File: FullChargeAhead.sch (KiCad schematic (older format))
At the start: 18 parts, among them P101 USB_OTG, P102 CONN_01X02, U101 MCP73834

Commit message: starting rev 2
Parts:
- removed D103: NOPOP, LEDs:LED_0805, symbol LED
- removed R106: NOPOP, Resistors_SMD:R_0805_HandSoldering, symbol R
- removed R108: 0R, Resistors_SMD:R_0805_HandSoldering, symbol R
- removed TH101: THERMISTOR, Resistors_ThroughHole:Resistor_Horizontal_RM10mm, symbol THERMISTOR
- added P102: CONN_01X02, Pin_Headers:Pin_Header_Straight_1x02, symbol CONN_01X02
- added R107: 1K, Resistors_SMD:R_0805_HandSoldering, symbol R
- P101: footprint Connect:USB_Micro-B_10103594-0001LF -> FullChargeAhead:USB_Micro-B_10103594-0001LF
- P103: renamed from P102; value CONN_01X02 -> JST_2PIN; footprint Connect:PINHEAD1-2 -> FullChargeAhead:JST_Type_PH_Side_Entry_1x02_Pitch2.00mm; MPN (none) -> S2B-PH-K-S(LF)(SN)
- U101: Fieldname (none) -> Value; MPN (none) -> MCP73834-FCI/UN
- renumbered R107 to R108, R109 to R110
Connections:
- net GND: now also P102.2 (P2)
- net at U101.7 (~TE): now also R107.1
- net at U101.8 (THERM): now also R110.2
- new net: P102.1 (P1), R107.2
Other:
- moved on the sheet: C102
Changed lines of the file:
@@
 Comp ""
 Comment1 "Note 1: R107 must be sized to match max charge rate of battery. 38.3K = 110mA at 4.2V"
-Comment2 "Note 2: Verify polarity of connection P102 matches polarity of battery connector"
-Comment3 "Note 3: Do we need a jumper to 1K and ground on ~TE?"
+Comment2 "Note 2: Verify polarity of connection P103 matches polarity of battery connector"
+Comment3 ""
 Comment4 ""
 $EndDescr
@@
 F 1 "MCP73834" H 5500 3650 60  0000 C CNN
 F 2 "Housings_SSOP:MSOP-10_3x3mm_Pitch0.5mm" H 5500 3350 60  0001 C CNN
-F 3 "" H 5500 3350 60  0000 C CNN
+F 3 "http://ww1.microchip.com/downloads/en/DeviceDoc/22005b.pdf" H 5500 3350 60  0001 C CNN
+F 4 "Value" H 5500 3350 60  0001 C CNN "Fieldname"
+F 5 "MCP73834-FCI/UN" H 5500 3350 60  0001 C CNN "MPN"
 	1    5500 3350
 	1    0    0    -1
 $EndComp
 $Comp
-L R R107
+L R R108
 U 1 1 57DAA130
 P 6400 3600
-F 0 "R107" V 6480 3600 50  0000 C CNN
+F 0 "R108" V 6480 3600 50  0000 C CNN
 F 1 "38.3R" V 6400 3600 39  0000 C CNN
 F 2 "Resistors_SMD:R_0805_HandSoldering" V 6330 3600 50  0001 C CNN
@@
 Wire Wire Line
 	6400 3750 6400 3900
-$Comp
-L R R108
-U 1 1 57DAA19D
-P 6650 3350
-F 0 "R108" V 6730 3350 50  0000 C CNN
-F 1 "0R" V 6650 3350 50  0000 C CNN
-F 2 "Resistors_SMD:R_0805_HandSoldering" V 6580 3350 50  0001 C CNN
-F 3 "" H 6650 3350 50  0000 C CNN
-	1    6650 3350
-	0    1    1    0
-$EndComp
-$Comp
-L R R109
-U 1 1 57DAA1D4
-P 6950 3700
-F 0 "R109" V 7030 3700 50  0000 C CNN
-F 1 "10K" V 6950 3700 50  0000 C CNN
-F 2 "Resistors_SMD:R_0805_HandSoldering" V 6880 3700 50  0001 C CNN
-F 3 "" H 6950 3700 50  0000 C CNN
-	1    6950 3700
-	-1   0    0    1
-$EndComp
-$Comp
-L R R106
-U 1 1 57DAA1FC
-P 4700 3650
-F 0 "R106" V 4780 3650 50  0000 C CNN
-F 1 "NOPOP" V 4700 3650 39  0000 C CNN
-F 2 "Resistors_SMD:R_0805_HandSoldering" V 4630 3650 50  0001 C CNN
-F 3 "" H 4700 3650 50  0000 C CNN
-	1    4700 3650
-	0    -1   -1   0
-$EndComp
-Wire Wire Line
-	5000 3550 4950 3550
-Wire Wire Line
-	4950 3550 4950 3650
-Wire Wire Line
-	4950 3650 4850 3650
 $Comp
 L R R105
@@
 Wire Wire Line
 	4850 3350 5000 3350
-Wire Wire Line
-	6000 3350 6500 3350
-Wire Wire Line
-	6800 3350 7350 3350
-Wire Wire Line
-	6950 3350 6950 3550
-$Comp
-L GND #PWR02
-U 1 1 57DAA375
-P 6950 3950
-F 0 "#PWR02" H 6950 3700 50  0001 C CNN
-F 1 "GND" H 6950 3800 50  0000 C CNN
-F 2 "" H 6950 3950 50  0000 C CNN
-F 3 "" H 6950 3950 50  0000 C CNN
-	1    6950 3950
-	1    0    0    -1
-$EndComp
-Wire Wire Line
-	6950 3850 6950 3950
-$Comp
-L THERMISTOR TH101
-U 1 1 57DAA3A8
-P 7350 3600
-F 0 "TH101" V 7450 3650 50  0000 C CNN
-F 1 "THERMISTOR" V 7250 3600 50  0000 C BNN
-F 2 "Resistors_ThroughHole:Resistor_Horizontal_RM10mm" H 7350 3600 50  0001 C CNN
-F 3 "" H 7350 3600 50  0000 C CNN
-	1    7350 3600
-	1    0    0    -1
-$EndComp
-Connection ~ 6950 3350
-$Comp
-L GND #PWR03
-U 1 1 57DAA46F
-P 7350 3950
-F 0 "#PWR03" H 7350 3700 50  0001 C CNN
-F 1 "GND" H 7350 3800 50  0000 C CNN
-F 2 "" H 7350 3950 50  0000 C CNN
-F 3 "" H 7350 3950 50  0000 C CNN
-	1    7350 3950
-	1    0    0    -1
-$EndComp
-Wire Wire Line
-	7350 3850 7350 3950
 $Comp
 L C C102
 U 1 1 57DAA4B0
-P 7750 3300
-F 0 "C102" H 7775 3400 50  0000 L CNN
-F 1 "4.7U" H 7775 3200 50  0000 L CNN
-F 2 "Capacitors_SMD:C_1206_HandSoldering" H 7788 3150 50  0001 C CNN
-F 3 "" H 7750 3300 50  0000 C CNN
-	1    7750 3300
-	1    0    0    -1
-$EndComp
-Wire Wire Line
-	6000 3150 8350 3150
+P 7300 3300
+F 0 "C102" H 7325 3400 50  0000 L CNN
+F 1 "4.7U" H 7325 3200 50  0000 L CNN
+F 2 "Capacitors_SMD:C_1206_HandSoldering" H 7338 3150 50  0001 C CNN
+F 3 "" H 7300 3300 50  0000 C CNN
+	1    7300 3300
+	1    0    0    -1
+$EndComp
+Wire Wire Line
+	6000 3150 6200 3150
+Wire Wire Line
+	6200 3150 7300 3150
+Wire Wire Line
+	7300 3150 8350 3150
 Wire Wire Line
 	6000 3250 6200 3250
@@
 L GND #PWR04
 U 1 1 57DAA520
-P 7750 3550
-F 0 "#PWR04" H 7750 3300 50  0001 C CNN
-F 1 "GND" H 7750 3400 50  0000 C CNN
-F 2 "" H 7750 3550 50  0000 C CNN
-F 3 "" H 7750 3550 50  0000 C CNN
-	1    7750 3550
-	1    0    0    -1
-$EndComp
-Wire Wire Line
-	7750 3450 7750 3550
-$Comp
-L CONN_01X02 P102
+P 7300 3550
+F 0 "#PWR04" H 7300 3300 50  0001 C CNN
+F 1 "GND" H 7300 3400 50  0000 C CNN
+F 2 "" H 7300 3550 50  0000 C CNN
+F 3 "" H 7300 3550 50  0000 C CNN
+	1    7300 3550
+	1    0    0    -1
+$EndComp
+Wire Wire Line
+	7300 3450 7300 3550
+$Comp
+L CONN_01X02 P103
 U 1 1 57DAA560
 P 8550 3200
-F 0 "P102" H 8550 3350 50  0000 C CNN
-F 1 "CONN_01X02" V 8700 3200 50  0000 C CNN
-F 2 "Connect:PINHEAD1-2" H 8550 3200 50  0001 C CNN
-F 3 "" H 8550 3200 50  0000 C CNN
+F 0 "P103" H 8550 3350 50  0000 C CNN
+F 1 "JST_2PIN" V 8700 3200 50  0000 C CNN
+F 2 "FullChargeAhead:JST_Type_PH_Side_Entry_1x02_Pitch2.00mm" H 8550 3200 50  0001 C CNN
+F 3 "http://www.jst-mfg.com/product/pdf/eng/ePH.pdf" H 8550 3200 50  0001 C CNN
+F 4 "S2B-PH-K-S(LF)(SN)" H 8550 3200 60  0001 C CNN "MPN"
 	1    8550 3200
 	1    0    0    -1
 $EndComp
-Connection ~ 7750 3150
+Connection ~ 7300 3150
 $Comp
 L GND #PWR05
@@
 Wire Wire Line
 	8350 3250 8350 3400
-$Comp
-L LED D103
-U 1 1 57DAA633
-P 4100 3750
-F 0 "D103" H 4100 3850 50  0000 C CNN
-F 1 "NOPOP" H 4100 3650 50  0000 C CNN
-F 2 "LEDs:LED_0805" H 4100 3750 50  0001 C CNN
-F 3 "" H 4100 3750 50  0000 C CNN
-F 4 "Value" H 4100 3750 60  0001 C CNN "Fieldname"
-	1    4100 3750
-	-1   0    0    1
-$EndComp
 $Comp
 L LED D102
@@
 	4550 3450 4300 3450
 Wire Wire Line
-	4550 3650 4300 3650
-Wire Wire Line
-	4300 3650 4300 3750
-Wire Wire Line
 	5000 2900 5000 3150
 Wire Wire Line
@@
 	3800 3450 3800 2900
 Connection ~ 3800 2900
-Wire Wire Line
-	3700 3750 3900 3750
-Wire Wire Line
-	3700 2800 3700 3750
-Connection ~ 3700 2900
 $Comp
 L C C101
@@
 F 0 "P101" V 3300 2650 50  0000 C CNN
 F 1 "USB_OTG" H 3000 2900 50  0000 C CNN
-F 2 "Connect:USB_Micro-B_10103594-0001LF" V 2950 2600 50  0001 C CNN
+F 2 "FullChargeAhead:USB_Micro-B_10103594-0001LF" V 2950 2600 50  0001 C CNN
 F 3 "http://portal.fciconnect.com/Comergent//fci/drawing/10103594.pdf" V 2950 2600 50  0001 C CNN
 F 4 "Value" H 3000 2700 60  0001 C CNN "Fieldname"
@@
 $EndComp
 Wire Wire Line
-	3300 2900 5000 2900
+	3300 2900 3450 2900
+Wire Wire Line
+	3450 2900 3700 2900
+Wire Wire Line
+	3700 2900 3800 2900
+Wire Wire Line
+	3800 2900 3900 2900
+Wire Wire Line
+	3900 2900 4050 2900
+Wire Wire Line
+	4050 2900 4400 2900
+Wire Wire Line
+	4400 2900 4900 2900
+Wire Wire Line
+	4900 2900 5000 2900
 Wire Wire Line
 	3300 2800 3400 2800
@@
 $EndComp
 Wire Wire Line
-	3300 2500 4700 2500
+	3300 2500 3550 2500
+Wire Wire Line
+	3550 2500 4700 2500
 Wire Wire Line
 	4050 2700 4050 2900
@@
 Vbat
 Wire Wire Line
-	6000 3550 6000 3850
-Wire Wire Line
-	6000 3850 6400 3850
-Connection ~ 6400 3850
+	6000 3550 6000 3900
 Wire Wire Line
 	3450 3000 3450 2900
@@
 Wire Wire Line
 	4850 3250 4850 3350
+$Comp
+L R R107
+U 1 1 57DB439E
+P 4750 3800
+F 0 "R107" V 4830 3800 50  0000 C CNN
+F 1 "1K" V 4750 3800 50  0000 C CNN
+F 2 "Resistors_SMD:R_0805_HandSoldering" V 4680 3800 50  0001 C CNN
+F 3 "" H 4750 3800 50  0000 C CNN
+	1    4750 3800
+	0    1    1    0
+$EndComp
+$Comp
+L CONN_01X02 P102
+U 1 1 57DB443B
+P 4300 3850
+F 0 "P102" H 4300 4000 50  0000 C CNN
+F 1 "CONN_01X02" V 4450 3850 50  0000 C CNN
+F 2 "Pin_Headers:Pin_Header_Straight_1x02" H 4300 3850 50  0001 C CNN
+F 3 "http://www.jst-mfg.com/product/pdf/eng/ePH.pdf" H 4300 3850 50  0001 C CNN
+F 4 "S2B-PH-K-S(LF)(SN)" H 4300 3850 60  0001 C CNN "MPN"
+	1    4300 3850
+	-1   0    0    -1
+$EndComp
+$Comp
+L GND #PWR08
+U 1 1 57DB4691
+P 4500 4000
+F 0 "#PWR08" H 4500 3750 50  0001 C CNN
+F 1 "GND" H 4500 3850 50  0000 C CNN
+F 2 "" H 4500 4000 50  0000 C CNN
+F 3 "" H 4500 4000 50  0000 C CNN
+	1    4500 4000
+	1    0    0    -1
+$EndComp
+Wire Wire Line
+	5000 3550 5000 3800
+Wire Wire Line
+	5000 3800 4900 3800
+Wire Wire Line
+	4600 3800 4500 3800
+Wire Wire Line
+	4500 3900 4500 4000
+Wire Wire Line
+	3700 2800 3700 2900
+Connection ~ 3700 2900
+$Comp
+L GND #PWR09
+U 1 1 57DC1683
+P 6000 3900
+F 0 "#PWR09" H 6000 3650 50  0001 C CNN
+F 1 "GND" H 6000 3750 50  0000 C CNN
+F 2 "" H 6000 3900 50  0000 C CNN
+F 3 "" H 6000 3900 50  0000 C CNN
+	1    6000 3900
+	1    0    0    -1
+$EndComp
+$Comp
+L GND #PWR02
+U 1 1 57DAA375
+P 6950 3950
+F 0 "#PWR02" H 6950 3700 50  0001 C CNN
+F 1 "GND" H 6950 3800 50  0000 C CNN
+F 2 "" H 6950 3950 50  0000 C CNN
+F 3 "" H 6950 3950 50  0000 C CNN
+	1    6950 3950
+	1    0    0    -1
+$EndComp
+Wire Wire Line
+	6950 3850 6950 3950
+$Comp
+L R R110
+U 1 1 57DAA1D4
+P 6950 3700
+F 0 "R110" V 7030 3700 50  0000 C CNN
+F 1 "10K" V 6950 3700 50  0000 C CNN
+F 2 "Resistors_SMD:R_0805_HandSoldering" V 6880 3700 50  0001 C CNN
+F 3 "" H 6950 3700 50  0000 C CNN
+	1    6950 3700
+	-1   0    0    1
+$EndComp
+Wire Wire Line
+	6000 3350 6950 3350
+Wire Wire Line
+	6950 3350 6950 3550
 $EndSCHEMATC

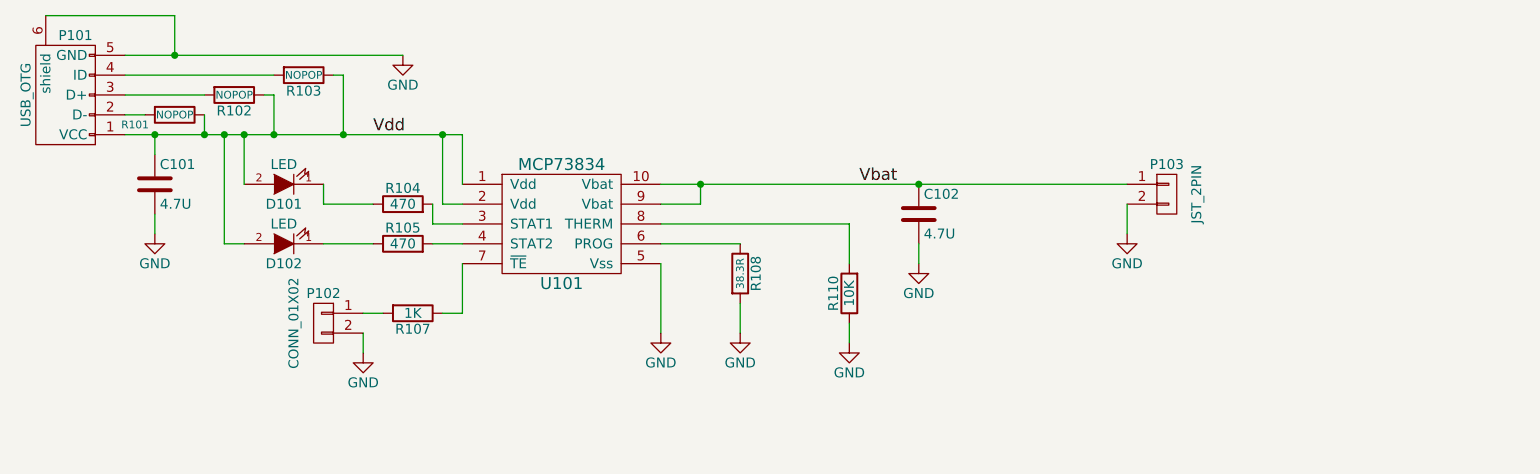
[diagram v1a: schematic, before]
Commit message: added Vbat connectors for current monitoring
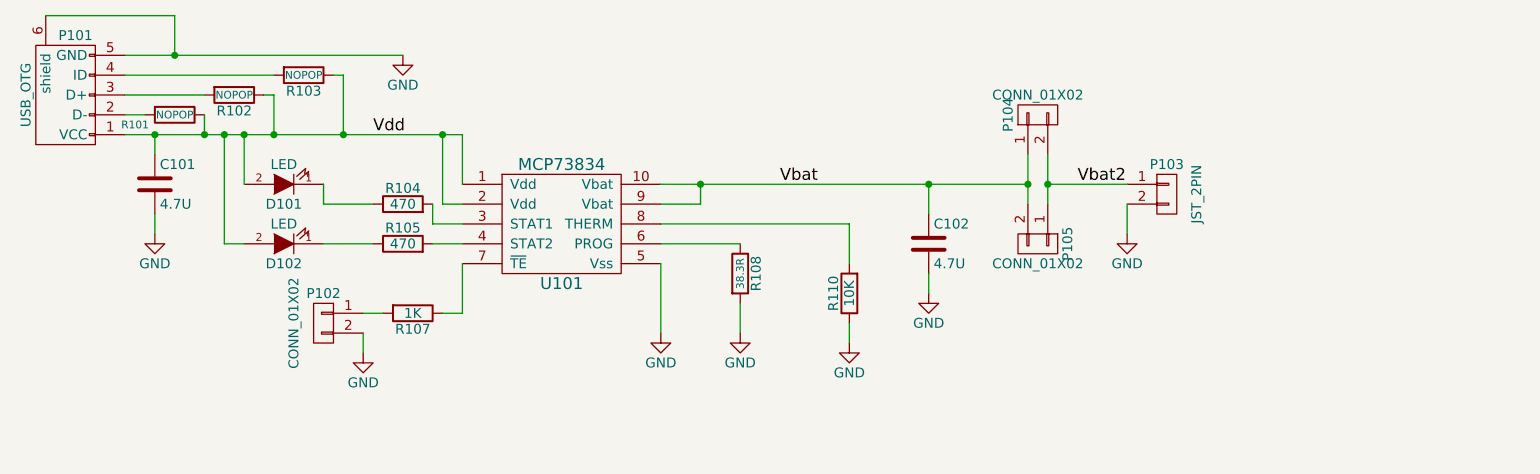
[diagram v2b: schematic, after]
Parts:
- added P104: CONN_01X02, Pin_Headers:Pin_Header_Straight_1x02, symbol CONN_01X02
- added P105: CONN_01X02, FullChargeAhead:Terminal_Block_200_mil, symbol CONN_01X02
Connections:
- net Vbat: now also P104.1 (P1), P105.2 (P2); no longer P103.1 (P1)
- new net Vbat2: P103.1 (P1), P104.2 (P2), P105.1 (P1)
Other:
- moved on the sheet: C102
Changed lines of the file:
@@
 L C C102
 U 1 1 57DAA4B0
-P 7300 3300
-F 0 "C102" H 7325 3400 50  0000 L CNN
-F 1 "4.7U" H 7325 3200 50  0000 L CNN
-F 2 "Capacitors_SMD:C_1206_HandSoldering" H 7338 3150 50  0001 C CNN
-F 3 "" H 7300 3300 50  0000 C CNN
-	1    7300 3300
-	1    0    0    -1
-$EndComp
-Wire Wire Line
-	6000 3150 6200 3150
-Wire Wire Line
-	6200 3150 7300 3150
-Wire Wire Line
-	7300 3150 8350 3150
+P 7350 3450
+F 0 "C102" H 7375 3550 50  0000 L CNN
+F 1 "4.7U" H 7375 3350 50  0000 L CNN
+F 2 "Capacitors_SMD:C_1206_HandSoldering" H 7388 3300 50  0001 C CNN
+F 3 "" H 7350 3450 50  0000 C CNN
+	1    7350 3450
+	1    0    0    -1
+$EndComp
 Wire Wire Line
 	6000 3250 6200 3250
-Wire Wire Line
-	6200 3250 6200 3150
-Connection ~ 6200 3150
-$Comp
-L GND #PWR04
+$Comp
+L GND #PWR02
 U 1 1 57DAA520
-P 7300 3550
-F 0 "#PWR04" H 7300 3300 50  0001 C CNN
-F 1 "GND" H 7300 3400 50  0000 C CNN
-F 2 "" H 7300 3550 50  0000 C CNN
-F 3 "" H 7300 3550 50  0000 C CNN
-	1    7300 3550
-	1    0    0    -1
-$EndComp
-Wire Wire Line
-	7300 3450 7300 3550
+P 7350 3700
+F 0 "#PWR02" H 7350 3450 50  0001 C CNN
+F 1 "GND" H 7350 3550 50  0000 C CNN
+F 2 "" H 7350 3700 50  0000 C CNN
+F 3 "" H 7350 3700 50  0000 C CNN
+	1    7350 3700
+	1    0    0    -1
+$EndComp
+Wire Wire Line
+	7350 3600 7350 3700
 $Comp
 L CONN_01X02 P103
@@
 	1    0    0    -1
 $EndComp
-Connection ~ 7300 3150
-$Comp
-L GND #PWR05
+$Comp
+L GND #PWR03
 U 1 1 57DAA5BC
 P 8350 3400
-F 0 "#PWR05" H 8350 3150 50  0001 C CNN
+F 0 "#PWR03" H 8350 3150 50  0001 C CNN
 F 1 "GND" H 8350 3250 50  0000 C CNN
 F 2 "" H 8350 3400 50  0000 C CNN
@@
 $EndComp
 $Comp
-L GND #PWR06
+L GND #PWR04
 U 1 1 57DAAAB6
 P 3450 3400
-F 0 "#PWR06" H 3450 3150 50  0001 C CNN
+F 0 "#PWR04" H 3450 3150 50  0001 C CNN
 F 1 "GND" H 3450 3250 50  0000 C CNN
 F 2 "" H 3450 3400 50  0000 C CNN
@@
 $EndComp
 Wire Wire Line
-	3300 2900 3450 2900
-Wire Wire Line
-	3450 2900 3700 2900
-Wire Wire Line
-	3700 2900 3800 2900
-Wire Wire Line
-	3800 2900 3900 2900
-Wire Wire Line
-	3900 2900 4050 2900
-Wire Wire Line
-	4050 2900 4400 2900
-Wire Wire Line
-	4400 2900 4900 2900
-Wire Wire Line
-	4900 2900 5000 2900
+	3300 2900 5000 2900
 Wire Wire Line
 	3300 2800 3400 2800
@@
 Connection ~ 4400 2900
 $Comp
-L GND #PWR07
+L GND #PWR05
 U 1 1 57DACC73
 P 4700 2500
-F 0 "#PWR07" H 4700 2250 50  0001 C CNN
+F 0 "#PWR05" H 4700 2250 50  0001 C CNN
 F 1 "GND" H 4700 2350 50  0000 C CNN
 F 2 "" H 4700 2500 50  0000 C CNN
@@
 $EndComp
 Wire Wire Line
-	3300 2500 3550 2500
-Wire Wire Line
-	3550 2500 4700 2500
+	3300 2500 4700 2500
 Wire Wire Line
 	4050 2700 4050 2900
 Text Label 4550 2900 0    60   ~ 0
 Vdd
-Text Label 7000 3150 0    60   ~ 0
-Vbat
 Wire Wire Line
 	6000 3550 6000 3900
@@
 $EndComp
 $Comp
-L GND #PWR08
+L GND #PWR06
 U 1 1 57DB4691
 P 4500 4000
-F 0 "#PWR08" H 4500 3750 50  0001 C CNN
+F 0 "#PWR06" H 4500 3750 50  0001 C CNN
 F 1 "GND" H 4500 3850 50  0000 C CNN
 F 2 "" H 4500 4000 50  0000 C CNN
@@
 Connection ~ 3700 2900
 $Comp
-L GND #PWR09
+L GND #PWR07
 U 1 1 57DC1683
 P 6000 3900
-F 0 "#PWR09" H 6000 3650 50  0001 C CNN
+F 0 "#PWR07" H 6000 3650 50  0001 C CNN
 F 1 "GND" H 6000 3750 50  0000 C CNN
 F 2 "" H 6000 3900 50  0000 C CNN
@@
 $EndComp
 $Comp
-L GND #PWR02
+L GND #PWR08
 U 1 1 57DAA375
 P 6950 3950
-F 0 "#PWR02" H 6950 3700 50  0001 C CNN
+F 0 "#PWR08" H 6950 3700 50  0001 C CNN
 F 1 "GND" H 6950 3800 50  0000 C CNN
 F 2 "" H 6950 3950 50  0000 C CNN
@@
 Wire Wire Line
 	6950 3350 6950 3550
+$Comp
+L CONN_01X02 P104
+U 1 1 57E203B6
+P 7900 2800
+F 0 "P104" H 7900 2950 50  0000 C CNN
+F 1 "CONN_01X02" V 8000 2800 50  0000 C CNN
+F 2 "Pin_Headers:Pin_Header_Straight_1x02" H 7900 2800 50  0001 C CNN
+F 3 "" H 7900 2800 50  0000 C CNN
+	1    7900 2800
+	0    -1   -1   0
+$EndComp
+$Comp
+L CONN_01X02 P105
+U 1 1 57E20401
+P 7900 3450
+F 0 "P105" H 7900 3600 50  0000 C CNN
+F 1 "CONN_01X02" V 8000 3450 50  0000 C CNN
+F 2 "FullChargeAhead:Terminal_Block_200_mil" H 7900 3450 50  0001 C CNN
+F 3 "" H 7900 3450 50  0000 C CNN
+	1    7900 3450
+	0    1    1    0
+$EndComp
+Wire Wire Line
+	6000 3150 7850 3150
+Wire Wire Line
+	7850 3000 7850 3250
+Wire Wire Line
+	7350 3300 7350 3150
+Connection ~ 7350 3150
+Wire Wire Line
+	6200 3250 6200 3150
+Connection ~ 6200 3150
+Connection ~ 7850 3150
+Wire Wire Line
+	7950 3000 7950 3250
+Wire Wire Line
+	8350 3150 7950 3150
+Connection ~ 7950 3150
+Text Label 6600 3150 0    60   ~ 0
+Vbat
+Text Label 8100 3150 0    60   ~ 0
+Vbat2
 $EndSCHEMATC

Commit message: added MPN for screw terminals
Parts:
- P105: MPN (none) -> OSTTC022162
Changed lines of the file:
@@
 F 2 "FullChargeAhead:Terminal_Block_200_mil" H 7900 3450 50  0001 C CNN
 F 3 "" H 7900 3450 50  0000 C CNN
+F 4 "OSTTC022162" H 7900 3450 60  0001 C CNN "MPN"
 	1    7900 3450
 	0    1    1    0
